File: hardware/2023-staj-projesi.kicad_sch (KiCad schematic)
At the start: 3 parts, among them J1 RELAY, J5 SENSOR, J6 POWER

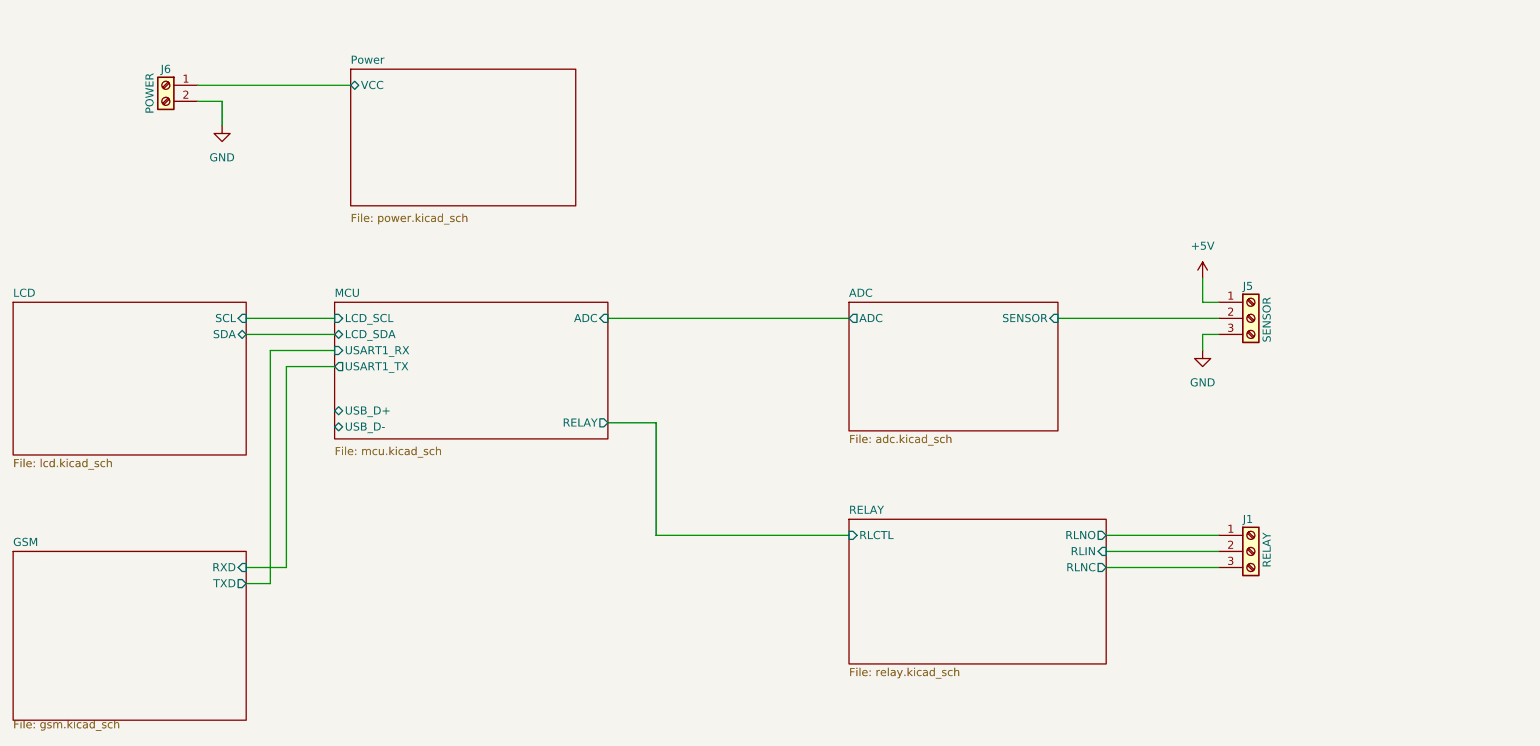
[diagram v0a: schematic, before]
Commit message: * 3V8 Power design fixed * Footprints assigned * Bom exported * PCB filter module placed
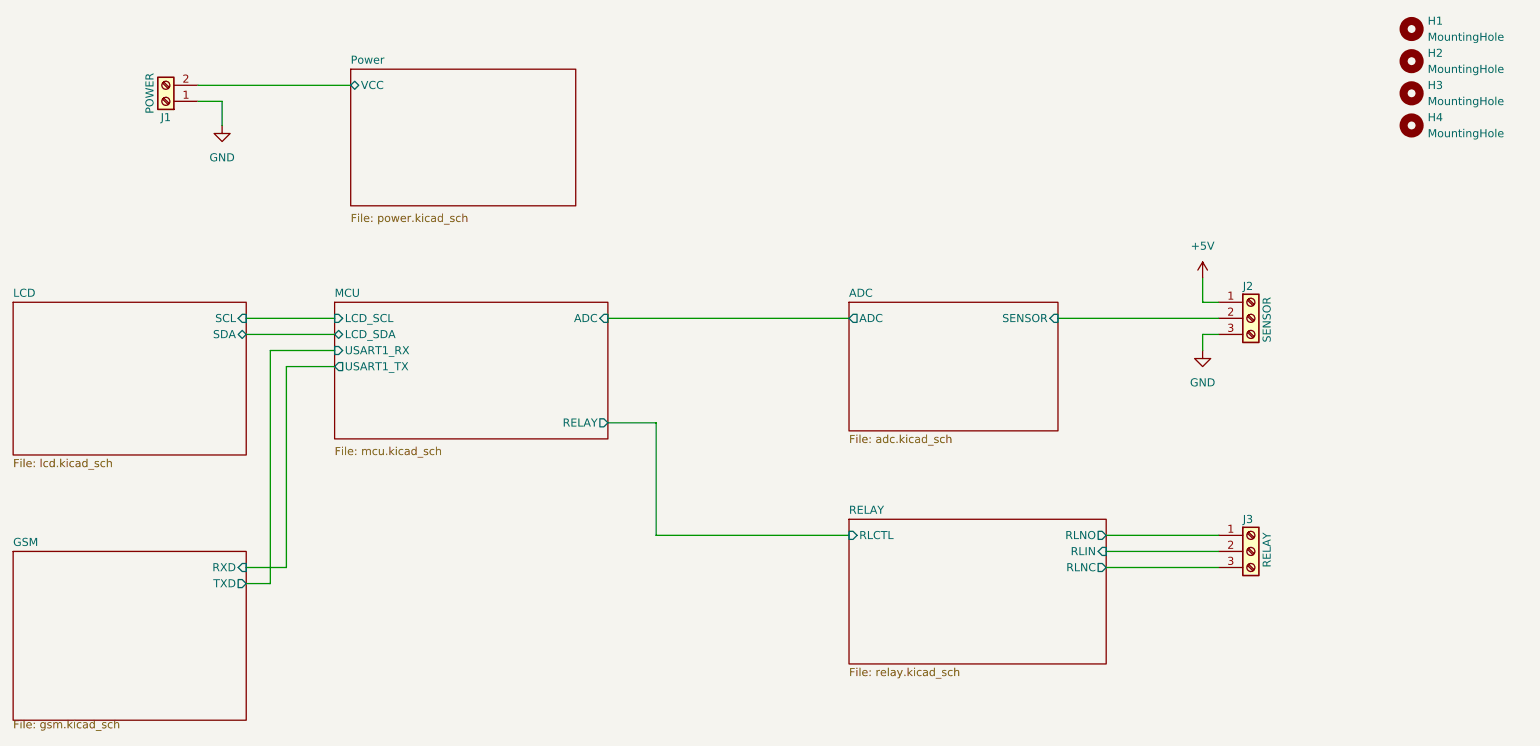
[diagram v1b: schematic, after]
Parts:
- added H1, H2, H3, H4: MountingHole, MountingHole:MountingHole_2.5mm_Pad, symbol Mechanical:MountingHole
- J1: renamed from J6; footprint (none) -> Connector_Phoenix_MSTB:PhoenixContact_MSTBA_2,5_2-G-5,08_1x02_P5.08mm_Horizontal
- J2: renamed from J5; footprint (none) -> Connector_Phoenix_MSTB:PhoenixContact_MSTBA_2,5_3-G-5,08_1x03_P5.08mm_Horizontal
- J3: renamed from J1; footprint (none) -> Connector_Phoenix_MSTB:PhoenixContact_MSTBA_2,5_3-G-5,08_1x03_P5.08mm_Horizontal
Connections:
- net GND: now also J1.1 (Pin_1); no longer J1.2 (Pin_2)
- net Power/VCC: now also J1.2 (Pin_2); no longer J1.1 (Pin_1)
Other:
- sheet MCU ports: added none; removed USB_D+, USB_D-
- moved on the sheet: J1
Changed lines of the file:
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@@
     (rev "1.0")
     (company "Hidro Elektronik")
+    (comment 1 "Mehmet Emre SAYGI(2019513057@ogr.cu.edu.tr)")
+    (comment 2 "Yilmaz Can DURAN(duranyilmazcan@gmail.com)")
+    (comment 3 "Asli VEZIR(vezirasli@gmail.com)")
   )
   (wire (pts (xy 135.89 100.33) (xy 166.37 100.33))
@@
   (symbol (lib_id "power:GND") (at 67.31 35.56 0) (unit 1)
     (in_bom yes) (on_board yes) (dnp no) (fields_autoplaced)
-    (property "Reference" "#PWR039" (at 67.31 41.91 0)
+    (property "Reference" "#PWR01" (at 67.31 41.91 0)
       (effects (font (size 1.27 1.27)) hide)
     )
@@
       (project "2023-staj-projesi"
         (path "/069db7ad-35cd-4aa8-8111-e026f632a4df"
-          (reference "#PWR039") (unit 1)
+          (reference "#PWR01") (unit 1)
+        )
+      )
+    )
+  )
+  (symbol (lib_id "Mechanical:MountingHole") (at 255.27 25.4 0) (unit 1)
+    (in_bom yes) (on_board yes) (dnp no) (fields_autoplaced)
+    (property "Reference" "H2" (at 257.81 24.13 0)
+      (effects (font (size 1.27 1.27)) (justify left))
+    )
+    (property "Value" "MountingHole" (at 257.81 26.67 0)
+      (effects (font (size 1.27 1.27)) (justify left))
+    )
+    (property "Footprint" "MountingHole:MountingHole_2.5mm_Pad" (at 255.27 25.4 0)
+      (effects (font (size 1.27 1.27)) hide)
+    )
+    (property "Datasheet" "~" (at 255.27 25.4 0)
+      (effects (font (size 1.27 1.27)) hide)
+    )
+    (instances
+      (project "2023-staj-projesi"
+        (path "/069db7ad-35cd-4aa8-8111-e026f632a4df"
+          (reference "H2") (unit 1)
+        )
+      )
+    )
+  )
+  (symbol (lib_id "Mechanical:MountingHole") (at 255.27 35.56 0) (unit 1)
+    (in_bom yes) (on_board yes) (dnp no) (fields_autoplaced)
+    (property "Reference" "H4" (at 257.81 34.29 0)
+      (effects (font (size 1.27 1.27)) (justify left))
+    )
+    (property "Value" "MountingHole" (at 257.81 36.83 0)
+      (effects (font (size 1.27 1.27)) (justify left))
+    )
+    (property "Footprint" "MountingHole:MountingHole_2.5mm_Pad" (at 255.27 35.56 0)
+      (effects (font (size 1.27 1.27)) hide)
+    )
+    (property "Datasheet" "~" (at 255.27 35.56 0)
+      (effects (font (size 1.27 1.27)) hide)
+    )
+    (instances
+      (project "2023-staj-projesi"
+        (path "/069db7ad-35cd-4aa8-8111-e026f632a4df"
+          (reference "H4") (unit 1)
         )
       )
@@
   (symbol (lib_id "power:GND") (at 222.25 71.12 0) (unit 1)
     (in_bom yes) (on_board yes) (dnp no) (fields_autoplaced)
-    (property "Reference" "#PWR037" (at 222.25 77.47 0)
+    (property "Reference" "#PWR03" (at 222.25 77.47 0)
       (effects (font (size 1.27 1.27)) hide)
     )
@@
       (project "2023-staj-projesi"
         (path "/069db7ad-35cd-4aa8-8111-e026f632a4df"
-          (reference "#PWR037") (unit 1)
-        )
-      )
-    )
-  )
-  (symbol (lib_id "Connector:Screw_Terminal_01x02") (at 58.42 29.21 0) (mirror y) (unit 1)
+          (reference "#PWR03") (unit 1)
+        )
+      )
+    )
+  )
+  (symbol (lib_id "Connector:Screw_Terminal_01x02") (at 58.42 31.75 180) (unit 1)
     (in_bom yes) (on_board yes) (dnp no)
-    (property "Reference" "J6" (at 58.42 26.67 0)
+    (property "Reference" "J1" (at 58.42 34.29 0)
       (effects (font (size 1.27 1.27)))
     )
@@
       (effects (font (size 1.27 1.27)))
     )
-    (property "Footprint" "" (at 58.42 29.21 0)
-      (effects (font (size 1.27 1.27)) hide)
-    )
-    (property "Datasheet" "~" (at 58.42 29.21 0)
+    (property "Footprint" "Connector_Phoenix_MSTB:PhoenixContact_MSTBA_2,5_2-G-5,08_1x02_P5.08mm_Horizontal" (at 58.42 31.75 0)
+      (effects (font (size 1.27 1.27)) hide)
+    )
+    (property "Datasheet" "~" (at 58.42 31.75 0)
       (effects (font (size 1.27 1.27)) hide)
     )
@@
       (project "2023-staj-projesi"
         (path "/069db7ad-35cd-4aa8-8111-e026f632a4df"
-          (reference "J6") (unit 1)
+          (reference "J1") (unit 1)
+        )
+      )
+    )
+  )
+  (symbol (lib_id "Mechanical:MountingHole") (at 255.27 20.32 0) (unit 1)
+    (in_bom yes) (on_board yes) (dnp no) (fields_autoplaced)
+    (property "Reference" "H1" (at 257.81 19.05 0)
+      (effects (font (size 1.27 1.27)) (justify left))
+    )
+    (property "Value" "MountingHole" (at 257.81 21.59 0)
+      (effects (font (size 1.27 1.27)) (justify left))
+    )
+    (property "Footprint" "MountingHole:MountingHole_2.5mm_Pad" (at 255.27 20.32 0)
+      (effects (font (size 1.27 1.27)) hide)
+    )
+    (property "Datasheet" "~" (at 255.27 20.32 0)
+      (effects (font (size 1.27 1.27)) hide)
+    )
+    (instances
+      (project "2023-staj-projesi"
+        (path "/069db7ad-35cd-4aa8-8111-e026f632a4df"
+          (reference "H1") (unit 1)
+        )
+      )
+    )
+  )
+  (symbol (lib_id "Mechanical:MountingHole") (at 255.27 30.48 0) (unit 1)
+    (in_bom yes) (on_board yes) (dnp no) (fields_autoplaced)
+    (property "Reference" "H3" (at 257.81 29.21 0)
+      (effects (font (size 1.27 1.27)) (justify left))
+    )
+    (property "Value" "MountingHole" (at 257.81 31.75 0)
+      (effects (font (size 1.27 1.27)) (justify left))
+    )
+    (property "Footprint" "MountingHole:MountingHole_2.5mm_Pad" (at 255.27 30.48 0)
+      (effects (font (size 1.27 1.27)) hide)
+    )
+    (property "Datasheet" "~" (at 255.27 30.48 0)
+      (effects (font (size 1.27 1.27)) hide)
+    )
+    (instances
+      (project "2023-staj-projesi"
+        (path "/069db7ad-35cd-4aa8-8111-e026f632a4df"
+          (reference "H3") (unit 1)
         )
       )
@@
   (symbol (lib_id "Connector:Screw_Terminal_01x03") (at 229.87 102.87 0) (unit 1)
     (in_bom yes) (on_board yes) (dnp no)
-    (property "Reference" "J1" (at 228.6 97.79 0)
+    (property "Reference" "J3" (at 228.6 97.79 0)
       (effects (font (size 1.27 1.27)) (justify left))
     )
@@
       (effects (font (size 1.27 1.27)) (justify left))
     )
-    (property "Footprint" "" (at 229.87 102.87 0)
+    (property "Footprint" "Connector_Phoenix_MSTB:PhoenixContact_MSTBA_2,5_3-G-5,08_1x03_P5.08mm_Horizontal" (at 229.87 102.87 0)
       (effects (font (size 1.27 1.27)) hide)
     )
@@
       (project "2023-staj-projesi"
         (path "/069db7ad-35cd-4aa8-8111-e026f632a4df"
-          (reference "J1") (unit 1)
+          (reference "J3") (unit 1)
         )
       )
@@
   (symbol (lib_id "Connector:Screw_Terminal_01x03") (at 229.87 66.04 0) (unit 1)
     (in_bom yes) (on_board yes) (dnp no)
-    (property "Reference" "J5" (at 228.6 60.96 0)
+    (property "Reference" "J2" (at 228.6 60.96 0)
       (effects (font (size 1.27 1.27)) (justify left))
     )
@@
       (effects (font (size 1.27 1.27)) (justify left))
     )
-    (property "Footprint" "" (at 229.87 66.04 0)
+    (property "Footprint" "Connector_Phoenix_MSTB:PhoenixContact_MSTBA_2,5_3-G-5,08_1x03_P5.08mm_Horizontal" (at 229.87 66.04 0)
       (effects (font (size 1.27 1.27)) hide)
     )
@@
       (project "2023-staj-projesi"
         (path "/069db7ad-35cd-4aa8-8111-e026f632a4df"
-          (reference "J5") (unit 1)
+          (reference "J2") (unit 1)
         )
       )
@@
   (symbol (lib_id "power:+5V") (at 222.25 59.69 0) (unit 1)
     (in_bom yes) (on_board yes) (dnp no) (fields_autoplaced)
-    (property "Reference" "#PWR038" (at 222.25 63.5 0)
+    (property "Reference" "#PWR02" (at 222.25 63.5 0)
       (effects (font (size 1.27 1.27)) hide)
     )
@@
       (project "2023-staj-projesi"
         (path "/069db7ad-35cd-4aa8-8111-e026f632a4df"
-          (reference "#PWR038") (unit 1)
+          (reference "#PWR02") (unit 1)
         )
       )
@@
       (effects (font (size 1.27 1.27)) (justify left))
     )
-    (pin "USB_D-" bidirectional (at 85.09 83.185 180)
-      (effects (font (size 1.27 1.27)) (justify left))
-    )
-    (pin "USB_D+" bidirectional (at 85.09 80.645 180)
-      (effects (font (size 1.27 1.27)) (justify left))
-    )

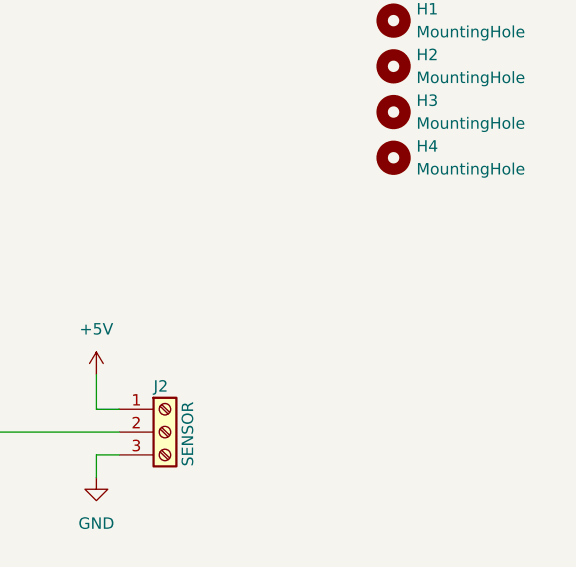
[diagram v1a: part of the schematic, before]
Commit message: Added PCB names and logos
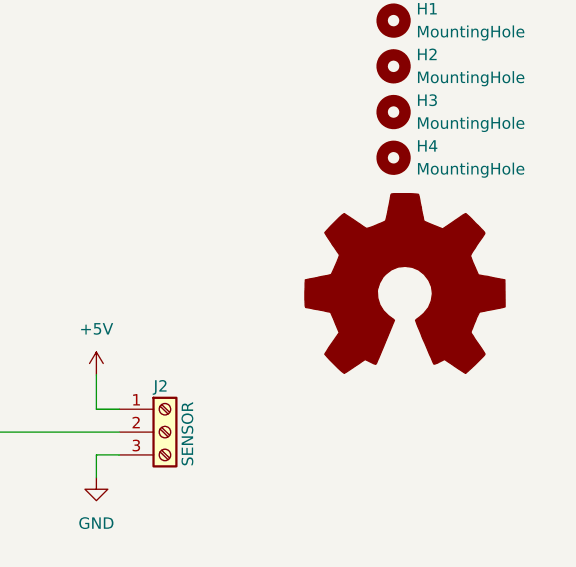
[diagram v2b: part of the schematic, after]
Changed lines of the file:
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@@
+    )
+  )
+  (symbol (lib_id "Graphic:Logo_Open_Hardware_Large") (at 256.54 50.8 0) (unit 1)
+    (in_bom no) (on_board no) (dnp no) (fields_autoplaced)
+    (property "Reference" "#SYM1" (at 256.54 38.1 0)
+      (effects (font (size 1.27 1.27)) hide)
+    )
+    (property "Value" "Logo_Open_Hardware_Large" (at 256.54 60.96 0)
+      (effects (font (size 1.27 1.27)) hide)
+    )
+    (property "Footprint" "Symbol:OSHW-Logo2_7.3x6mm_SilkScreen" (at 256.54 50.8 0)
+      (effects (font (size 1.27 1.27)) hide)
+    )
+    (property "Datasheet" "~" (at 256.54 50.8 0)
+      (effects (font (size 1.27 1.27)) hide)
+    )
+    (property "Sim.Enable" "0" (at 256.54 50.8 0)
+      (effects (font (size 1.27 1.27)) hide)
+    )
+    (instances
+      (project "2023-staj-projesi"
+        (path "/069db7ad-35cd-4aa8-8111-e026f632a4df"
+          (reference "#SYM1") (unit 1)
+        )
+      )
     )
   )
